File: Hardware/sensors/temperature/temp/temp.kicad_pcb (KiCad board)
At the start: 2 copper layers, 17.3 x 7.2 mm, 3 parts, among them J1 Conn_01x03_Socket, J2 Conn_01x03_Socket, U1 TMP1826DGK

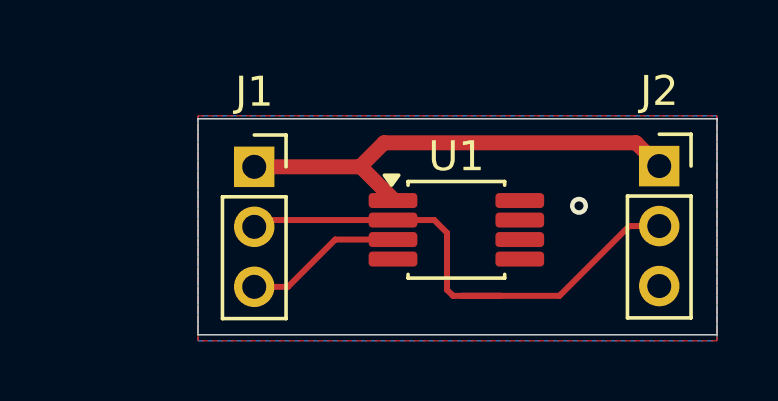
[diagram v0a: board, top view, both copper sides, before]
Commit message: improved temperature 1-wire pcb
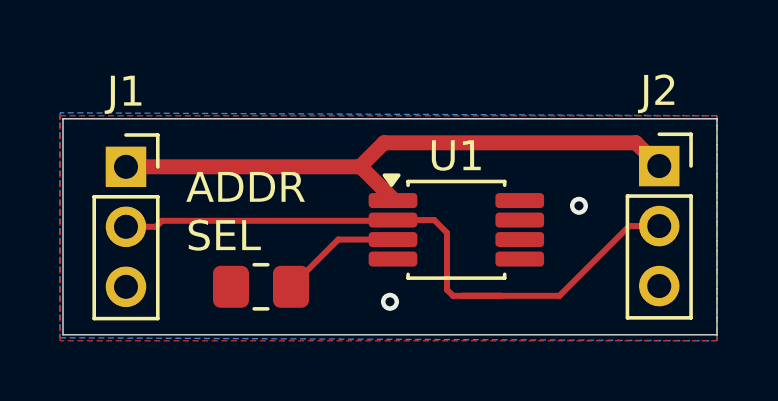
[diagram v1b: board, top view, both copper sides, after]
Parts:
- added R1: R, Resistor_SMD:R_0805_2012Metric_Pad1.20x1.40mm_HandSolder, F.Cu at (128.3, 83.5)
- moved J1 4.27 mm to (123.8, 79.5)
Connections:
- U1 pad 3: GND -> Net-(U1-ADDR)
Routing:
- net GND: track 5.28 -> 0.28 mm, vias 1 -> 2
- net Net-(J1-Pin_2): track 18.0 -> 22.3 mm
- net +3.3V: track 15.7 -> 20.0 mm
- net Net-(U1-ADDR): track 0.00 -> 4.05 mm
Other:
- board size 17.3 x 7.2 mm -> 21.8 x 7.2 mm
- board text added: "ADDR SEL"
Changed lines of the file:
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@@
 	(net 2 "GND")
 	(net 3 "+3.3V")
+	(net 4 "Net-(U1-ADDR)")
 	(footprint "Connector_PinSocket_2.00mm:PinSocket_1x03_P2.00mm_Vertical"
 		(layer "F.Cu")
-		(at 128.075 79.5)
+		(at 123.8 79.5)
 		(descr "Through hole straight socket strip, 1x03, 2.00mm pitch, single row (from Kicad 4.0.7), script generated")
 		(tags "Through hole socket strip THT 1x03 2.00mm single row")
@@
 		)
 	)
+	(footprint "Resistor_SMD:R_0805_2012Metric_Pad1.20x1.40mm_HandSolder"
+		(layer "F.Cu")
+		(at 128.3 83.5 180)
+		(descr "Resistor SMD 0805 (2012 Metric), square (rectangular) end terminal, IPC-7351 nominal with elongated pad for handsoldering. (Body size source: IPC-SM-782 page 72, https://www.pcb-3d.com/wordpress/wp-content/uploads/ipc-sm-782a_amendment_1_and_2.pdf), generated with kicad-footprint-generator")
+		(tags "resistor handsolder")
+		(property "Reference" "R1"
+			(at 0 -1.65 0)
+			(layer "F.SilkS")
+			(hide yes)
+			(effects
+				(font
+					(size 1 1)
+					(thickness 0.15)
+				)
+			)
+		)
+		(property "Value" "R"
+			(at 0 1.65 0)
+			(layer "F.Fab")
+			(effects
+				(font
+					(size 1 1)
+					(thickness 0.15)
+				)
+			)
+		)
+		(property "Datasheet" "~"
+			(at 0 0 0)
+			(layer "F.Fab")
+			(hide yes)
+			(effects
+				(font
+					(size 1.27 1.27)
+					(thickness 0.15)
+				)
+			)
+		)
+		(property "Description" "Resistor"
+			(at 0 0 0)
+			(layer "F.Fab")
+			(hide yes)
+			(effects
+				(font
+					(size 1.27 1.27)
+					(thickness 0.15)
+				)
+			)
+		)
+		(property ki_fp_filters "R_*")
+		(sheetname "/")
+		(sheetfile "temp.kicad_sch")
+		(attr smd)
+		(fp_line
+			(start -0.227064 0.735)
+			(end 0.227064 0.735)
+			(stroke
+				(width 0.12)
+				(type solid)
+			)
+			(layer "F.SilkS")
+		)
+		(fp_line
+			(start -0.227064 -0.735)
+			(end 0.227064 -0.735)
+			(stroke
+				(width 0.12)
+				(type solid)
+			)
+			(layer "F.SilkS")
+		)
+		(fp_rect
+			(start -1.85 -0.95)
+			(end 1.85 0.95)
+			(stroke
+				(width 0.05)
+				(type solid)
+			)
+			(fill no)
+			(layer "F.CrtYd")
+		)
+		(fp_rect
+			(start -1 -0.625)
+			(end 1 0.625)
+			(stroke
+				(width 0.1)
+				(type solid)
+			)
+			(fill no)
+			(layer "F.Fab")
+		)
+		(fp_text user "${REFERENCE}"
+			(at 0 0 0)
+			(layer "F.Fab")
+			(effects
+				(font
+					(size 0.5 0.5)
+					(thickness 0.08)
+				)
+			)
+		)
+		(pad "1" smd roundrect
+			(at -1 0 180)
+			(size 1.2 1.4)
+			(layers "F.Cu" "F.Mask" "F.Paste")
+			(roundrect_rratio 0.208333)
+			(net 4 "Net-(U1-ADDR)")
+			(pintype "passive")
+		)
+		(pad "2" smd roundrect
+			(at 1 0 180)
+			(size 1.2 1.4)
+			(layers "F.Cu" "F.Mask" "F.Paste")
+			(roundrect_rratio 0.208333)
+			(net 2 "GND")
+			(pintype "passive")
+		)
+		(embedded_fonts no)
+		(model "${KICAD9_3DMODEL_DIR}/Resistor_SMD.3dshapes/R_0805_2012Metric.step"
+			(offset
+				(xyz 0 0 0)
+			)
+			(scale
+				(xyz 1 1 1)
+			)
+			(rotate
+				(xyz 0 0 0)
+			)
+		)
+	)
 	(footprint "Package_SO:VSSOP-8_3x3mm_P0.65mm"
 		(layer "F.Cu")
@@
 			(layers "F.Cu" "F.Mask" "F.Paste")
 			(roundrect_rratio 0.25)
-			(net 2 "GND")
+			(net 4 "Net-(U1-ADDR)")
 			(pinfunction "ADDR")
 			(pintype "input")
@@
 	)
 	(gr_rect
-		(start 126.2 77.9)
+		(start 121.7 77.9)
 		(end 143.5 85.1)
 		(stroke
@@
 		(layer "Edge.Cuts")
 	)
+	(gr_text "ADDR\nSEL"
+		(at 125.8 82.4 0)
+		(layer "F.SilkS")
+		(effects
+			(font
+				(size 1 1)
+				(thickness 0.1)
+			)
+			(justify left bottom)
+		)
+	)
 	(segment
 		(start 136.3 83.8)
@@
 	)
 	(segment
-		(start 128.3 81.275)
-		(end 132.7 81.275)
-		(width 0.2)
-		(layer "F.Cu")
-		(net 1)
-	)
-	(segment
 		(start 138.25 83.8)
 		(end 136.3 83.8)
@@
 	)
 	(segment
+		(start 132.675 81.3)
+		(end 125 81.3)
+		(width 0.2)
+		(layer "F.Cu")
+		(net 1)
+	)
+	(segment
 		(start 132.7 81.275)
 		(end 134.075 81.275)
@@
 	)
 	(segment
-		(start 128.075 81.5)
-		(end 128.3 81.275)
-		(width 0.2)
-		(layer "F.Cu")
-		(net 1)
-	)
-	(segment
 		(start 134.5 81.7)
 		(end 134.5 83.6)
@@
 	)
 	(segment
+		(start 124.8 81.5)
+		(end 123.8 81.5)
+		(width 0.2)
+		(layer "F.Cu")
+		(net 1)
+	)
+	(segment
 		(start 134.7 83.8)
 		(end 136.3 83.8)
@@
 	)
 	(segment
+		(start 132.7 81.275)
+		(end 132.675 81.3)
+		(width 0.2)
+		(layer "F.Cu")
+		(net 1)
+	)
+	(segment
+		(start 125 81.3)
+		(end 124.8 81.5)
+		(width 0.2)
+		(layer "F.Cu")
+		(net 1)
+	)
+	(segment
 		(start 138.25 83.8)
 		(end 140.575 81.475)
@@
 	)
 	(segment
-		(start 128.075 83.5)
-		(end 129.2 83.5)
-		(width 0.2)
-		(layer "F.Cu")
-		(net 2)
-	)
-	(segment
-		(start 129.2 83.5)
-		(end 130.775 81.925)
-		(width 0.2)
-		(layer "F.Cu")
-		(net 2)
-	)
-	(segment
-		(start 130.775 81.925)
-		(end 132.7 81.925)
+		(start 127.4 83.5)
+		(end 127.2 83.7)
 		(width 0.2)
 		(layer "F.Cu")
@@
 		(net 2)
 	)
+	(via
+		(at 132.6 84)
+		(size 0.6)
+		(drill 0.3)
+		(layers "F.Cu" "B.Cu")
+		(free yes)
+		(net 2)
+	)
 	(segment
 		(start 131.625 79.5)
@@
 	)
 	(segment
-		(start 128.075 79.5)
-		(end 131.625 79.5)
-		(width 0.5)
-		(layer "F.Cu")
-		(net 3)
-	)
-	(segment
 		(start 140.8 78.7)
 		(end 141.575 79.475)
@@
 		(layer "F.Cu")
 		(net 3)
+	)
+	(segment
+		(start 131.625 79.5)
+		(end 123.8 79.5)
+		(width 0.5)
+		(layer "F.Cu")
+		(net 3)
+	)
+	(segment
+		(start 129.3 83.5)
+		(end 130.875 81.925)
+		(width 0.2)
+		(layer "F.Cu")
+		(net 4)
+	)
+	(segment
+		(start 130.875 81.925)
+		(end 132.7 81.925)
+		(width 0.2)
+		(layer "F.Cu")
+		(net 4)
 	)
 	(zone
@@
 		(polygon
 			(pts
-				(xy 126.2 77.8) (xy 143.5 77.8) (xy 143.5 85.3) (xy 126.2 85.3)
+				(xy 121.6 77.8) (xy 143.5 77.8) (xy 143.5 85.3) (xy 121.6 85.3)
 			)
 		)
@@
 		(polygon
 			(pts
-				(xy 143.5 77.8) (xy 126.2 77.8) (xy 126.2 85.3) (xy 143.5 85.3)
-			)
-		)
+				(xy 143.5 77.8) (xy 121.6 77.7) (xy 121.6 85.2) (xy 143.5 85.3)
+			)
+		)
